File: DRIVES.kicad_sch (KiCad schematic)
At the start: 0 parts

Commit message: lsd circuit in place
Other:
- added sheet LSD_01 (LSD.kicad_sch)
- added sheet LSD_23 (LSD.kicad_sch)

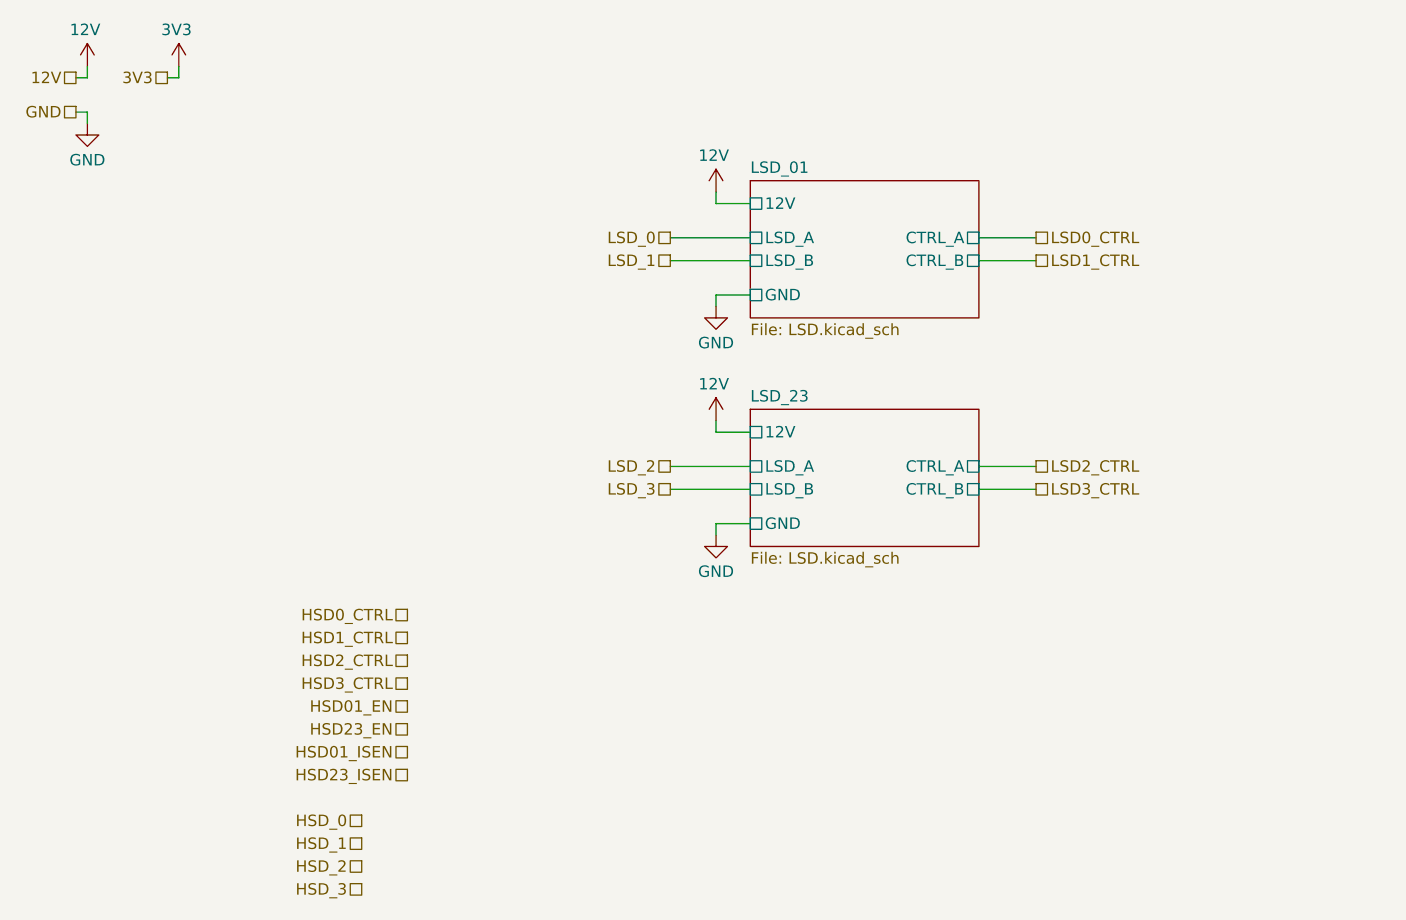
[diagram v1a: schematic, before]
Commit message: routed drives
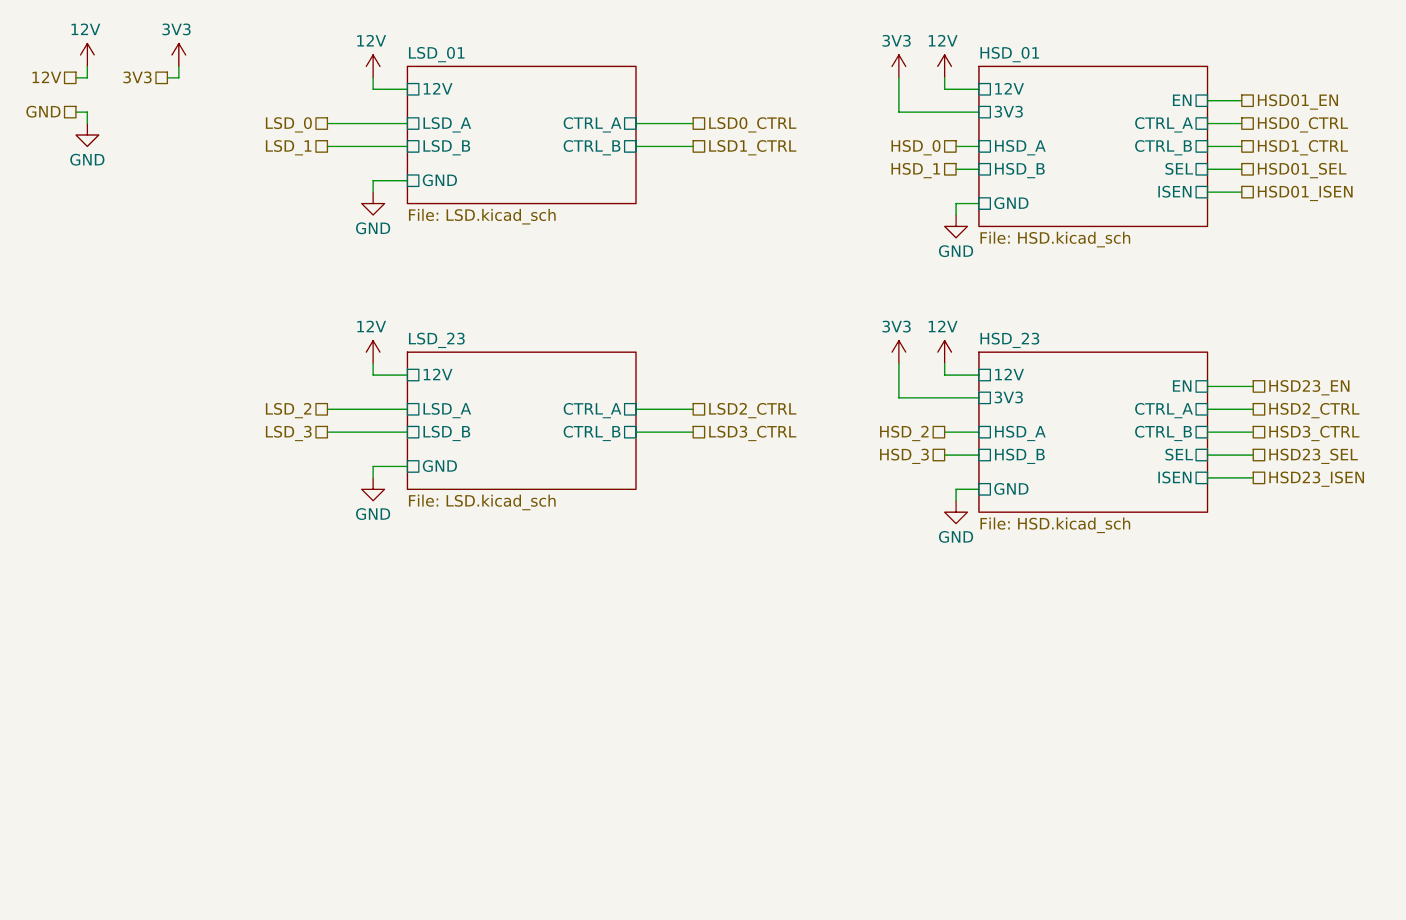
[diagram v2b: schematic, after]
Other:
- added sheet HSD_01 (HSD.kicad_sch)
- added sheet HSD_23 (HSD.kicad_sch)
